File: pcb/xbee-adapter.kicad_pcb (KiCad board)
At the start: 2 copper layers, 35.2 x 29.5 mm, 12 parts, among them J1 MCU, J2 Indicator, M1 DIGI_XBEE

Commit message: Adds resistors for the indicator LEDs
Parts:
- added R1: 270Ω, Resistor_SMD:R_0805_2012Metric, F.Cu at (144.1, 66.1)
- added R2: 270Ω, Resistor_SMD:R_0805_2012Metric, F.Cu at (144.1, 70.1)
- moved Lg2 7.62 mm to (133.1, 57.7)
- moved Lg1 0.76 mm to (135.6, 71.9)
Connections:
- M1 pad 13: /ON/SLEEP -> Net-(M1-ON/SLEEP)
- M1 pad 15: /ASSOCIATE -> Net-(M1-Associate/DIO5/AD5)
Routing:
- net /ASSOCIATE: track 16.2 -> 13.5 mm
- net Net-(M1-Associate/DIO5/AD5): track 0.00 -> 2.46 mm
- net Net-(M1-ON/SLEEP): track 0.00 -> 2.43 mm
- net /ON/SLEEP: track 11.8 -> 9.75 mm
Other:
- board text added: "LPS-X-1 Rev 1.1"
- board text removed: "LPS-X-1 Rev 1.0"
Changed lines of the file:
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@@
   )
   (paper "A4")
+  (title_block
+    (title "LPS-X-1 Leawood Power Sensor XBee Adapter 1.")
+    (date "2024-01-30")
+    (rev "1.1")
+  )
   (layers
     (0 "F.Cu" signal)
@@
   (net 19 "unconnected-(M1-AD1{slash}DIO1-Pad19)")
   (net 20 "unconnected-(M1-AD0{slash}DIO0{slash}Commission_PB-Pad20)")
+  (net 21 "Net-(M1-ON{slash}SLEEP)")
+  (net 22 "Net-(M1-Associate{slash}DIO5{slash}AD5)")
   (footprint "MountingHole:MountingHole_2.7mm_M2.5_DIN965" (layer "F.Cu")
     (at 120.65 56.388)
@@
       (net 14 "unconnected-(M1-~{CTS}{slash}DIO7-Pad12)") (pinfunction "~{CTS}/DIO7") (pintype "input+no_connect"))
     (pad "13" thru_hole circle (at 10.9982 14.0462) (size 1.524 1.524) (drill 0.762) (layers "*.Cu" "*.Mask")
-      (net 7 "/ON{slash}SLEEP") (pinfunction "ON/SLEEP") (pintype "input"))
+      (net 21 "Net-(M1-ON{slash}SLEEP)") (pinfunction "ON/SLEEP") (pintype "input"))
     (pad "14" thru_hole circle (at 10.9982 12.0396) (size 1.524 1.524) (drill 0.762) (layers "*.Cu" "*.Mask")
       (net 15 "unconnected-(M1-VREF-Pad14)") (pinfunction "VREF") (pintype "input+no_connect"))
     (pad "15" thru_hole circle (at 10.9982 10.033) (size 1.524 1.524) (drill 0.762) (layers "*.Cu" "*.Mask")
-      (net 8 "/ASSOCIATE") (pinfunction "Associate/DIO5/AD5") (pintype "input"))
+      (net 22 "Net-(M1-Associate{slash}DIO5{slash}AD5)") (pinfunction "Associate/DIO5/AD5") (pintype "input"))
     (pad "16" thru_hole circle (at 10.9982 8.0264) (size 1.524 1.524) (drill 0.762) (layers "*.Cu" "*.Mask")
       (net 16 "unconnected-(M1-~{RTS}{slash}DIO6-Pad16)") (pinfunction "~{RTS}/DIO6") (pintype "input+no_connect"))
@@
   )
   (footprint "Symbol:KiCad-Logo2_5mm_SilkScreen" (layer "F.Cu")
-    (at 136.398 71.882)
+    (at 135.636 71.882)
     (descr "KiCad Logo")
     (tags "Logo KiCad")
@@
       (stroke (width 0.15) (type solid)) (layer "Dwgs.User"))
   )
+  (footprint "Resistor_SMD:R_0805_2012Metric" (layer "F.Cu")
+    (at 144.145 70.0805 -90)
+    (descr "Resistor SMD 0805 (2012 Metric), square (rectangular) end terminal, IPC_7351 nominal, (Body size source: IPC-SM-782 page 72, https://www.pcb-3d.com/wordpress/wp-content/uploads/ipc-sm-782a_amendment_1_and_2.pdf), generated with kicad-footprint-generator")
+    (tags "resistor")
+    (property "Sheetfile" "xbee-adapter.kicad_sch")
+    (property "Sheetname" "")
+    (property "ki_description" "Resistor")
+    (property "ki_keywords" "R res resistor")
+    (attr smd)
+    (fp_text reference "R2" (at 2.6905 -0.127 90) (layer "F.SilkS")
+        (effects (font (size 1 1) (thickness 0.15)))
+    )
+    (fp_text value "270Ω" (at 0 1.65 90) (layer "F.Fab") hide
+        (effects (font (size 1 1) (thickness 0.15)))
+    )
+    (fp_text user "${REFERENCE}" (at 0 0 90) (layer "F.Fab")
+        (effects (font (size 0.5 0.5) (thickness 0.08)))
+    )
+    (fp_line (start -0.227064 -0.735) (end 0.227064 -0.735)
+      (stroke (width 0.12) (type solid)) (layer "F.SilkS"))
+    (fp_line (start -0.227064 0.735) (end 0.227064 0.735)
+      (stroke (width 0.12) (type solid)) (layer "F.SilkS"))
+    (fp_line (start -1.68 -0.95) (end 1.68 -0.95)
+      (stroke (width 0.05) (type solid)) (layer "F.CrtYd"))
+    (fp_line (start -1.68 0.95) (end -1.68 -0.95)
+      (stroke (width 0.05) (type solid)) (layer "F.CrtYd"))
+    (fp_line (start 1.68 -0.95) (end 1.68 0.95)
+      (stroke (width 0.05) (type solid)) (layer "F.CrtYd"))
+    (fp_line (start 1.68 0.95) (end -1.68 0.95)
+      (stroke (width 0.05) (type solid)) (layer "F.CrtYd"))
+    (fp_line (start -1 -0.625) (end 1 -0.625)
+      (stroke (width 0.1) (type solid)) (layer "F.Fab"))
+    (fp_line (start -1 0.625) (end -1 -0.625)
+      (stroke (width 0.1) (type solid)) (layer "F.Fab"))
+    (fp_line (start 1 -0.625) (end 1 0.625)
+      (stroke (width 0.1) (type solid)) (layer "F.Fab"))
+    (fp_line (start 1 0.625) (end -1 0.625)
+      (stroke (width 0.1) (type solid)) (layer "F.Fab"))
+    (pad "1" smd roundrect (at -0.9125 0 270) (size 1.025 1.4) (layers "F.Cu" "F.Paste" "F.Mask") (roundrect_rratio 0.243902)
+      (net 21 "Net-(M1-ON{slash}SLEEP)") (pintype "passive"))
+    (pad "2" smd roundrect (at 0.9125 0 270) (size 1.025 1.4) (layers "F.Cu" "F.Paste" "F.Mask") (roundrect_rratio 0.243902)
+      (net 7 "/ON{slash}SLEEP") (pintype "passive"))
+    (model "${KICAD6_3DMODEL_DIR}/Resistor_SMD.3dshapes/R_0805_2012Metric.wrl"
+      (offset (xyz 0 0 0))
+      (scale (xyz 1 1 1))
+      (rotate (xyz 0 0 0))
+    )
+  )
   (footprint "Connector_PinHeader_2.54mm:PinHeader_2x03_P2.54mm_Vertical" (layer "F.Cu")
     (at 130.302 78.74 -90)
@@
     (pad "" np_thru_hole circle (at 0 0) (size 2.7 2.7) (drill 2.7) (layers "*.Cu" "*.Mask"))
   )
+  (footprint "Resistor_SMD:R_0805_2012Metric" (layer "F.Cu")
+    (at 144.145 66.1435 -90)
+    (descr "Resistor SMD 0805 (2012 Metric), square (rectangular) end terminal, IPC_7351 nominal, (Body size source: IPC-SM-782 page 72, https://www.pcb-3d.com/wordpress/wp-content/uploads/ipc-sm-782a_amendment_1_and_2.pdf), generated with kicad-footprint-generator")
+    (tags "resistor")
+    (property "Sheetfile" "xbee-adapter.kicad_sch")
+    (property "Sheetname" "")
+    (property "ki_description" "Resistor")
+    (property "ki_keywords" "R res resistor")
+    (attr smd)
+    (fp_text reference "R1" (at -2.7705 0 90) (layer "F.SilkS")
+        (effects (font (size 1 1) (thickness 0.15)))
+    )
+    (fp_text value "270Ω" (at 0 1.65 90) (layer "F.Fab") hide
+        (effects (font (size 1 1) (thickness 0.15)))
+    )
+    (fp_text user "${REFERENCE}" (at 0 0 90) (layer "F.Fab")
+        (effects (font (size 0.5 0.5) (thickness 0.08)))
+    )
+    (fp_line (start -0.227064 -0.735) (end 0.227064 -0.735)
+      (stroke (width 0.12) (type solid)) (layer "F.SilkS"))
+    (fp_line (start -0.227064 0.735) (end 0.227064 0.735)
+      (stroke (width 0.12) (type solid)) (layer "F.SilkS"))
+    (fp_line (start -1.68 -0.95) (end 1.68 -0.95)
+      (stroke (width 0.05) (type solid)) (layer "F.CrtYd"))
+    (fp_line (start -1.68 0.95) (end -1.68 -0.95)
+      (stroke (width 0.05) (type solid)) (layer "F.CrtYd"))
+    (fp_line (start 1.68 -0.95) (end 1.68 0.95)
+      (stroke (width 0.05) (type solid)) (layer "F.CrtYd"))
+    (fp_line (start 1.68 0.95) (end -1.68 0.95)
+      (stroke (width 0.05) (type solid)) (layer "F.CrtYd"))
+    (fp_line (start -1 -0.625) (end 1 -0.625)
+      (stroke (width 0.1) (type solid)) (layer "F.Fab"))
+    (fp_line (start -1 0.625) (end -1 -0.625)
+      (stroke (width 0.1) (type solid)) (layer "F.Fab"))
+    (fp_line (start 1 -0.625) (end 1 0.625)
+      (stroke (width 0.1) (type solid)) (layer "F.Fab"))
+    (fp_line (start 1 0.625) (end -1 0.625)
+      (stroke (width 0.1) (type solid)) (layer "F.Fab"))
+    (pad "1" smd roundrect (at -0.9125 0 270) (size 1.025 1.4) (layers "F.Cu" "F.Paste" "F.Mask") (roundrect_rratio 0.243902)
+      (net 22 "Net-(M1-Associate{slash}DIO5{slash}AD5)") (pintype "passive"))
+    (pad "2" smd roundrect (at 0.9125 0 270) (size 1.025 1.4) (layers "F.Cu" "F.Paste" "F.Mask") (roundrect_rratio 0.243902)
+      (net 8 "/ASSOCIATE") (pintype "passive"))
+    (model "${KICAD6_3DMODEL_DIR}/Resistor_SMD.3dshapes/R_0805_2012Metric.wrl"
+      (offset (xyz 0 0 0))
+      (scale (xyz 1 1 1))
+      (rotate (xyz 0 0 0))
+    )
+  )
   (footprint "MountingHole:MountingHole_2.7mm_M2.5_DIN965" (layer "F.Cu")
     (at 150.495 80.264)
@@
   )
   (footprint "sjm-mechanical:MyBasic_rounded_50_1" (layer "F.Cu")
-    (at 133.35 65.278)
+    (at 133.096 57.658)
     (property "Sheetfile" "xbee-adapter.kicad_sch")
     (property "Sheetname" "")
@@
   (gr_rect (start 117.983 53.594) (end 153.162 83.058)
     (stroke (width 0.1) (type default)) (fill none) (layer "Edge.Cuts"))
-  (gr_text "LPS-X-1 \nRev 1.0" (at 135.89 68.326) (layer "B.SilkS")
+  (gr_text "LPS-X-1 \nRev 1.1" (at 135.89 68.326) (layer "B.SilkS")
     (effects (font (size 1.016 1.016) (thickness 0.254) bold) (justify left bottom mirror))
   )
-  (gr_text "LPS-X-1 \nRev 1.0" (at 137.287 67.564) (layer "F.SilkS")
+  (gr_text "LPS-X-1 \nRev 1.1" (at 137.033 59.944) (layer "F.SilkS")
     (effects (font (size 1.016 1.016) (thickness 0.254) bold) (justify left bottom))
   )
@@
   (segment (start 127.762 74.3458) (end 124.5616 71.1454) (width 0.25) (layer "F.Cu") (net 5))
   (segment (start 127.762 78.74) (end 127.762 74.3458) (width 0.25) (layer "F.Cu") (net 5))
-  (segment (start 145.923 80.01) (end 145.073 79.16) (width 0.25) (layer "F.Cu") (net 7))
-  (segment (start 145.073 79.16) (end 145.073 70.6238) (width 0.25) (layer "F.Cu") (net 7))
-  (segment (start 145.073 70.6238) (end 146.558 69.1388) (width 0.25) (layer "F.Cu") (net 7))
-  (segment (start 143.383 68.3006) (end 146.558 65.1256) (width 0.25) (layer "F.Cu") (net 8))
-  (segment (start 143.383 80.01) (end 143.383 68.3006) (width 0.25) (layer "F.Cu") (net 8))
+  (segment (start 144.145 78.232) (end 145.923 80.01) (width 0.25) (layer "F.Cu") (net 7))
+  (segment (start 144.145 70.993) (end 144.145 78.232) (width 0.25) (layer "F.Cu") (net 7))
+  (segment (start 143.12 68.081) (end 143.12 79.747) (width 0.25) (layer "F.Cu") (net 8))
+  (segment (start 144.145 67.056) (end 143.12 68.081) (width 0.25) (layer "F.Cu") (net 8))
+  (segment (start 143.12 79.747) (end 143.383 80.01) (width 0.25) (layer "F.Cu") (net 8))
+  (segment (start 144.1742 69.1388) (end 144.145 69.168) (width 0.25) (layer "F.Cu") (net 21))
+  (segment (start 146.558 69.1388) (end 144.1742 69.1388) (width 0.25) (layer "F.Cu") (net 21))
+  (segment (start 144.2504 65.1256) (end 144.145 65.231) (width 0.25) (layer "F.Cu") (net 22))
+  (segment (start 146.558 65.1256) (end 144.2504 65.1256) (width 0.25) (layer "F.Cu") (net 22))
   (zone (net 6) (net_name "GND") (layer "F.Cu") (hatch edge 0.5)
     (connect_pads (clearance 0.1524))

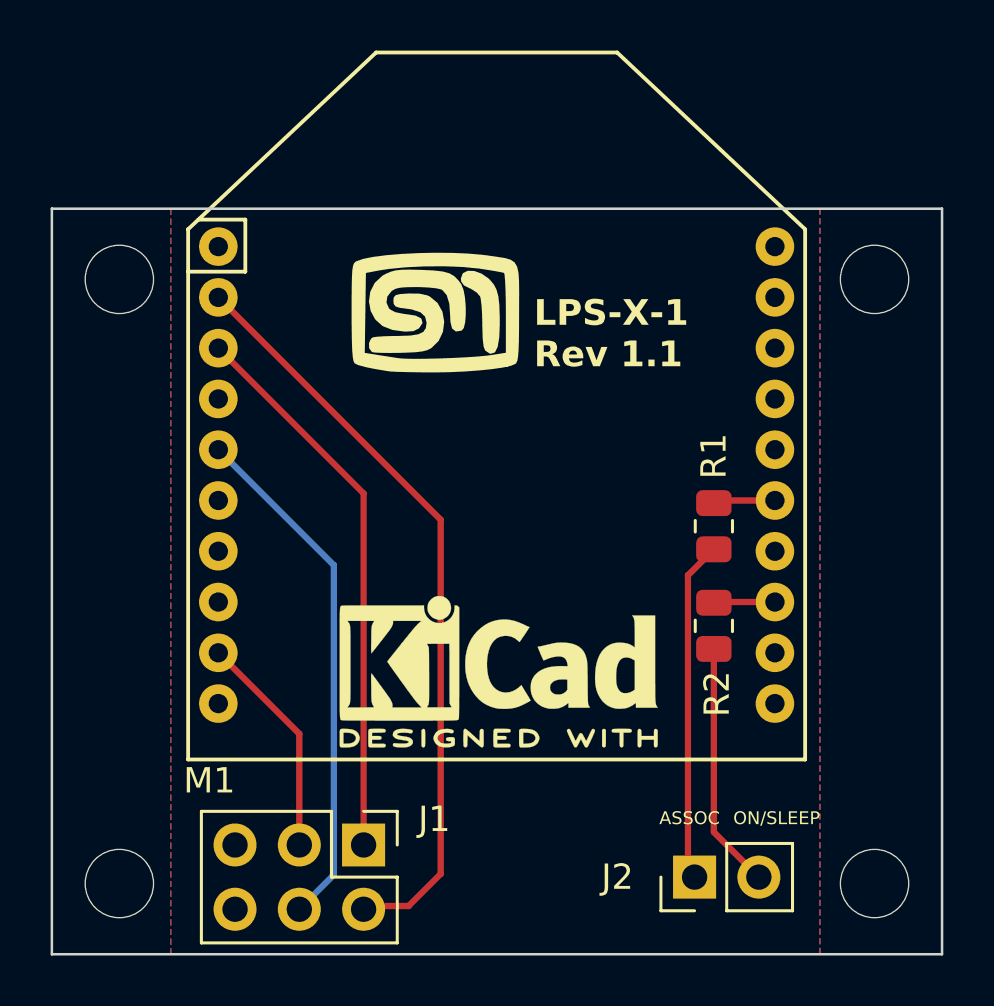
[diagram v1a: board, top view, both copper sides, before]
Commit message: Adds a ground pin for the inticator connector
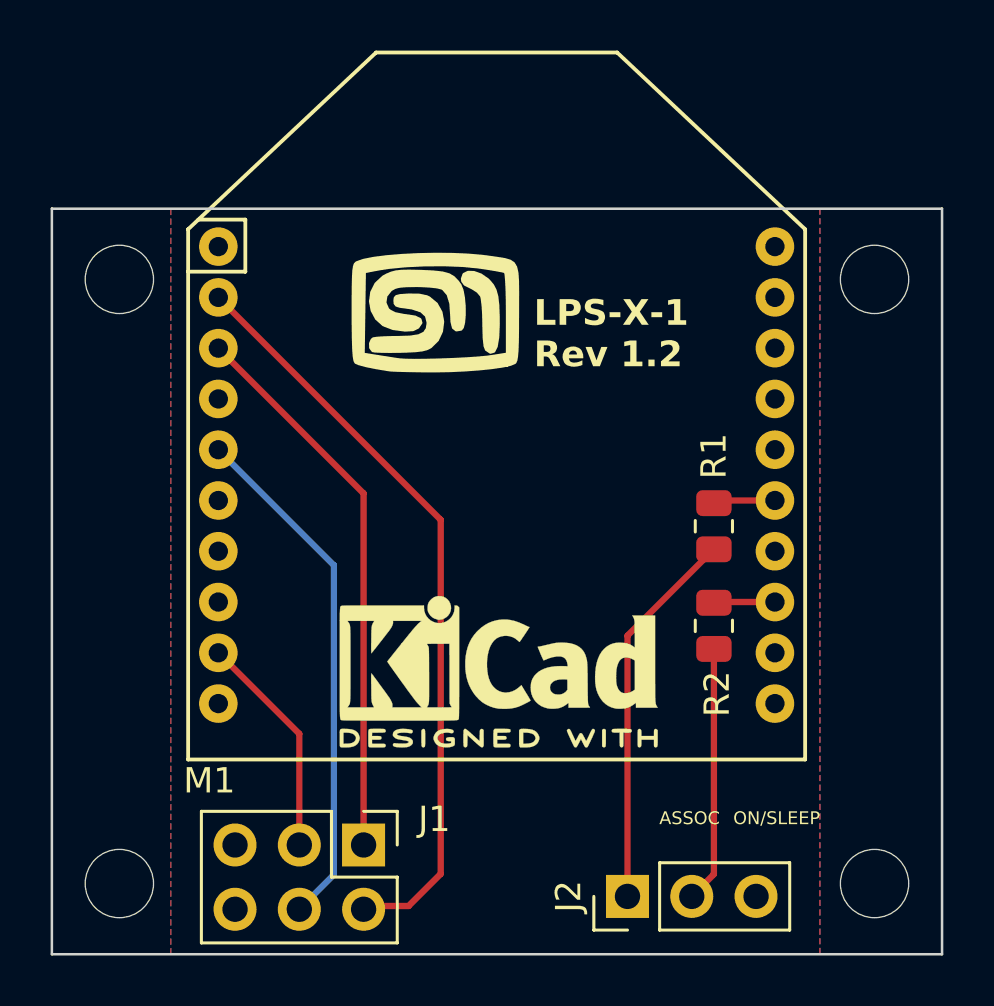
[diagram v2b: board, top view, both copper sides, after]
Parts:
- J2: footprint Connector_PinHeader_2.54mm:PinHeader_1x02_P2.54mm_Vertical -> Connector_PinHeader_2.54mm:PinHeader_1x03_P2.54mm_Vertical
- moved J2 2.76 mm to (140.7, 80.8)
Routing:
- net /ASSOCIATE: track 13.5 -> 15.1 mm
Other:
- board text added: "LPS-X-1 Rev 1.2"
- board text removed: "LPS-X-1 Rev 1.1"
